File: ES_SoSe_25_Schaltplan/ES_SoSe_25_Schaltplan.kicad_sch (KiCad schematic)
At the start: 3 parts

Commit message: updated scematic
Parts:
- added U3, U4: ~, symbol es_custom_symbols:SSD1806
- added U5: ~, symbol es_custom_symbols:74HC595
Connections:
- net at A1.11 (D8): now also U5.4 (SCLK)
- net at A1.12 (D9): now also U5.5 (LOAD)
- net at A1.13 (D10): now also U5.3 (SDI)
- net at A1.19 (A0): now also U2.H2 (H)
- net at A1.20 (A1): now also U2.V2 (V)
- net at A1.21 (A2): now also U1.H2 (H)
- net at A1.22 (A3): now also U1.V2 (V)
- net at A1.23 (SDA/A4): now also U3.1 (SDA), U4.1 (SDA)
- net at A1.24 (SCL/A5): now also U3.2 (SCL), U4.2 (SCL)
- net GND: now reaches A1.29 (GND), A1.4 (GND)
- net GND: now also U1.B2A (SEL-), U1.H3 (H-), U1.V3 (V-), U2.B2A (SEL-), U2.H3 (H-), U2.V3 (V-), U3.3 (GND), U4.3 (GND), U5.2 (GND)
- net VCC: now reaches A1.30 (VIN)
- net VCC: now also U1.H1 (H+), U1.V1 (V+), U2.H1 (H+), U2.V1 (V+), U3.4 (Vcc), U4.4 (Vcc), U5.1 (Vcc)
- net at A1.5 (D2): now also U1.B1A (Sel+)
- net at A1.6 (D3): now also U2.B1A (Sel+)
- no-connect marks 2 -> 3
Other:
- note added: "Dashboard Schaltplan"
- note added: "I2C"
- note added: "Joysticks"
- moved on the sheet: A1, U1, U2

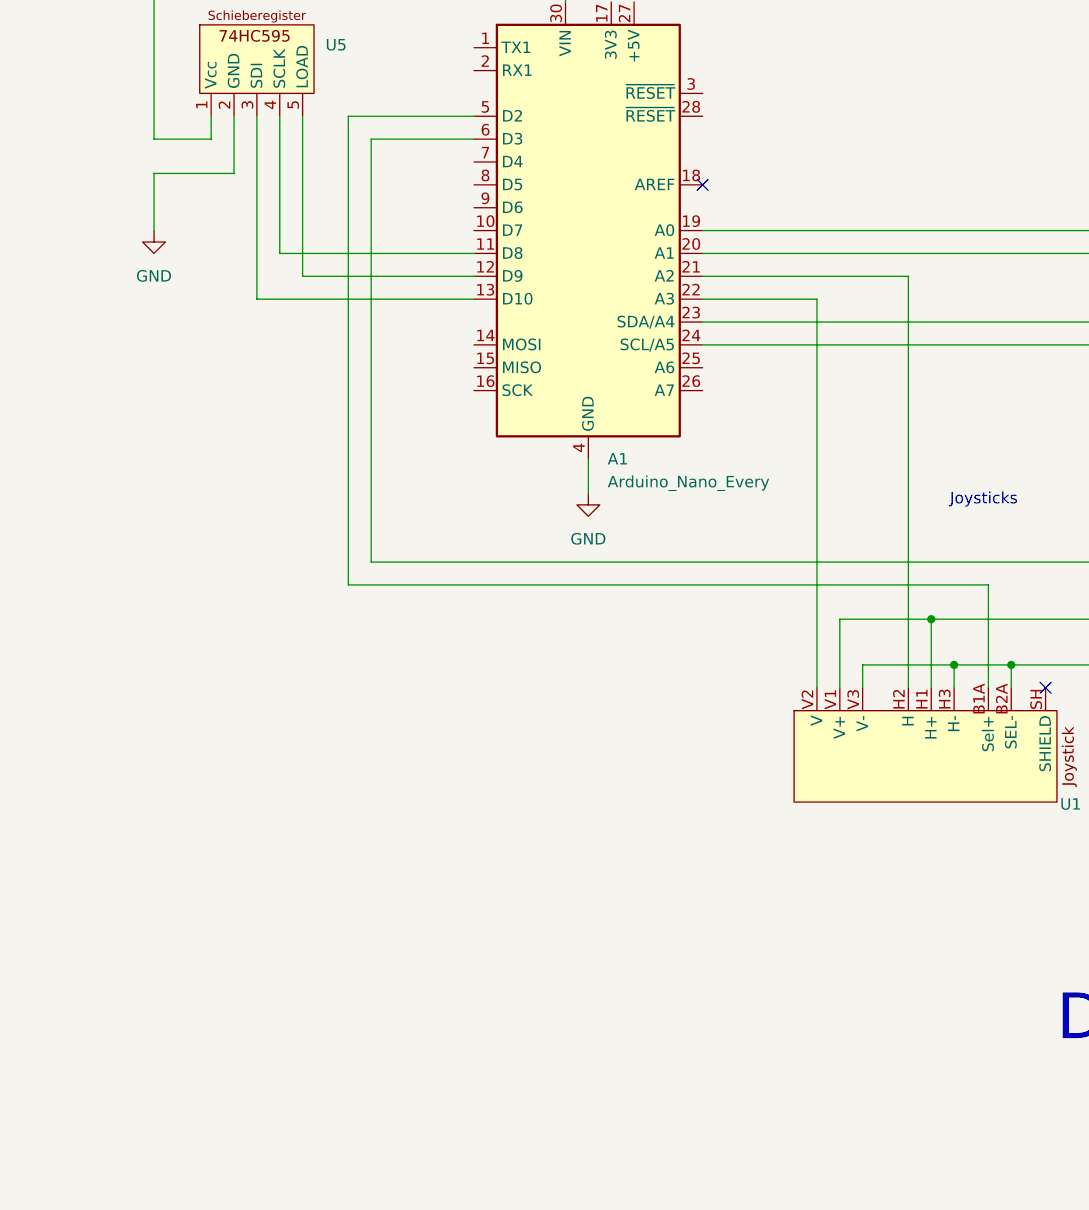
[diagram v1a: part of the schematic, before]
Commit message: added BLE LED
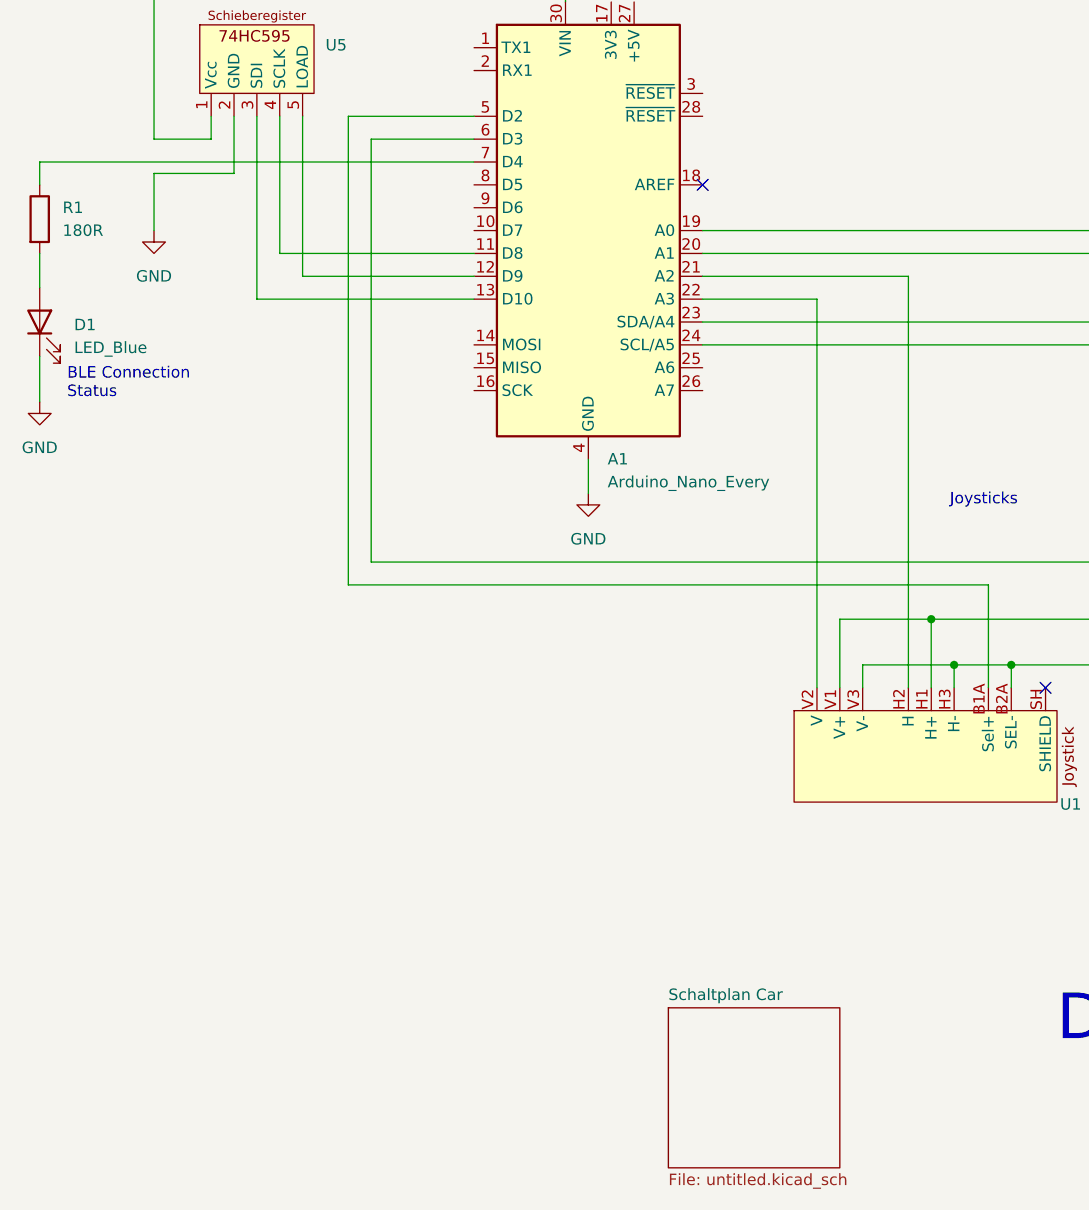
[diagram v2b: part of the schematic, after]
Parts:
- added D1: LED_Blue, symbol Device:LED
- added R1: 180R, symbol Device:R
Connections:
- net GND: now also D1.1 (K)
- net at A1.7 (D4): now also R1.1
- new net: D1.2 (A), R1.2
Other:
- added sheet Schaltplan Car (untitled.kicad_sch)
- note added: "BLE Connection Status"

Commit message: updated scematic
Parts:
- removed A1: Arduino_Nano_Every, Module:Arduino_Nano, symbol MCU_Module:Arduino_Nano_Every
- added A4: Arduino_Nano_33_BLE_Sense_Tile, PCM_arduino-library:Arduino_Nano_Every_Tile, symbol arduino-library:Arduino_Nano_33_BLE_Sense_Tile
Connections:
- net GND: now also A4.GND1 (GND), A4.GND2 (GND)
- net VCC: now also A4.VIN
- net at R1.1: now also A4.D4
- net at U5.4 (SCLK): now also A4.D8
- net at U5.5 (LOAD): now also A4.D9
- net at U5.3 (SDI): now also A4.D10
- net at U2.H2 (H): now also A4.A3
- net at U2.V2 (V): now also A4.A2
- net at U1.H2 (H): now also A4.A1
- net at U1.V2 (V): now also A4.A0
- net at U3.1 (SDA), U4.1 (SDA): now also A4.A4 (A4/SDA)
- net at U3.2 (SCL), U4.2 (SCL): now also A4.A5 (A5/SCL)
- net at U1.B1A (Sel+): now also A4.D2
- net at U2.B1A (Sel+): now also A4.D3
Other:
- moved on the sheet: U3, U4, U5

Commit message: adjusted scematic
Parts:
- removed U5: ~, symbol es_custom_symbols:74HC595
- added U5: ~, symbol es_custom_symbols:SSD1806
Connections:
- net GND: now also U5.3 (GND)
- net VCC: now also U5.4 (Vcc)
- net at A4.D8: now also U5.2 (SCL)
- net at A4.D9: now also U5.1 (SDA)
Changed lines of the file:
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@@
+	(wire
+		(pts
+			(xy 110.49 63.5) (xy 110.49 60.96)
+		)
+		(stroke
+			(width 0)
+			(type default)
+		)
+	)
 	(wire
 		(pts
@@
 	(wire
 		(pts
+			(xy 91.44 73.66) (xy 91.44 52.07)
+		)
+		(stroke
+			(width 0)
+			(type default)
+		)
+	)
+	(wire
+		(pts
 			(xy 118.11 123.19) (xy 118.11 58.42)
 		)
@@
 	(wire
 		(pts
+			(xy 95.25 52.07) (xy 95.25 71.12)
+		)
+		(stroke
+			(width 0)
+			(type default)
+		)
+	)
+	(wire
+		(pts
 			(xy 186.69 120.65) (xy 186.69 81.28)
 		)
@@
 	(wire
 		(pts
-			(xy 101.6 55.88) (xy 101.6 73.66)
-		)
-		(stroke
-			(width 0)
-			(type default)
-		)
-	)
-	(wire
-		(pts
 			(xy 228.6 50.8) (xy 228.6 71.12)
 		)
@@
 	(wire
 		(pts
-			(xy 101.6 73.66) (xy 121.92 73.66)
-		)
-		(stroke
-			(width 0)
-			(type default)
-		)
-	)
-	(wire
-		(pts
 			(xy 209.55 137.16) (xy 209.55 134.62)
 		)
@@
 	(wire
 		(pts
-			(xy 91.44 55.88) (xy 91.44 58.42)
-		)
-		(stroke
-			(width 0)
-			(type default)
-		)
-	)
-	(wire
-		(pts
 			(xy 259.08 58.42) (xy 233.68 58.42)
 		)
@@
 	(wire
 		(pts
-			(xy 96.52 55.88) (xy 96.52 76.2)
+			(xy 95.25 71.12) (xy 121.92 71.12)
 		)
 		(stroke
@@
 	(wire
 		(pts
-			(xy 99.06 55.88) (xy 99.06 71.12)
-		)
-		(stroke
-			(width 0)
-			(type default)
-		)
-	)
-	(wire
-		(pts
 			(xy 236.22 121.92) (xy 236.22 129.54)
 		)
@@
 	(wire
 		(pts
-			(xy 85.09 62.23) (xy 85.09 68.58)
+			(xy 91.44 73.66) (xy 121.92 73.66)
 		)
 		(stroke
@@
 	(wire
 		(pts
+			(xy 110.49 57.15) (xy 104.14 57.15)
+		)
+		(stroke
+			(width 0)
+			(type default)
+		)
+	)
+	(wire
+		(pts
 			(xy 180.34 129.54) (xy 170.18 129.54)
 		)
@@
 	(wire
 		(pts
-			(xy 93.98 62.23) (xy 93.98 55.88)
+			(xy 110.49 60.96) (xy 100.33 60.96)
 		)
 		(stroke
@@
 	(wire
 		(pts
-			(xy 85.09 41.91) (xy 85.09 58.42)
+			(xy 100.33 60.96) (xy 100.33 52.07)
+		)
+		(stroke
+			(width 0)
+			(type default)
+		)
+	)
+	(wire
+		(pts
+			(xy 110.49 46.99) (xy 110.49 57.15)
 		)
 		(stroke
@@
 	(wire
 		(pts
-			(xy 99.06 71.12) (xy 121.92 71.12)
-		)
-		(stroke
-			(width 0)
-			(type default)
-		)
-	)
-	(wire
-		(pts
 			(xy 217.17 58.42) (xy 217.17 63.5)
 		)
@@
 	(wire
 		(pts
+			(xy 104.14 57.15) (xy 104.14 52.07)
+		)
+		(stroke
+			(width 0)
+			(type default)
+		)
+	)
+	(wire
+		(pts
 			(xy 204.47 78.74) (xy 172.72 78.74)
 		)
@@
 	(wire
 		(pts
-			(xy 96.52 76.2) (xy 121.92 76.2)
-		)
-		(stroke
-			(width 0)
-			(type default)
-		)
-	)
-	(wire
-		(pts
-			(xy 85.09 58.42) (xy 91.44 58.42)
-		)
-		(stroke
-			(width 0)
-			(type default)
-		)
-	)
-	(wire
-		(pts
 			(xy 118.11 123.19) (xy 223.52 123.19)
-		)
-		(stroke
-			(width 0)
-			(type default)
-		)
-	)
-	(wire
-		(pts
-			(xy 85.09 62.23) (xy 93.98 62.23)
 		)
 		(stroke
@@
 	(symbol
 		(lib_id "power:GND")
-		(at 85.09 68.58 0)
+		(at 110.49 63.5 0)
 		(unit 1)
 		(exclude_from_sim no)
@@
 		(fields_autoplaced yes)
 		(property "Reference" "#PWR04"
-			(at 85.09 74.93 0)
+			(at 110.49 69.85 0)
 			(effects
 				(font
@@
 		)
 		(property "Value" "GND"
-			(at 85.09 73.66 0)
+			(at 110.49 68.58 0)
 			(effects
 				(font
@@
 		)
 		(property "Footprint" ""
-			(at 85.09 68.58 0)
+			(at 110.49 63.5 0)
 			(effects
 				(font
@@
 		)
 		(property "Datasheet" ""
-			(at 85.09 68.58 0)
+			(at 110.49 63.5 0)
 			(effects
 				(font
@@
 		)
 		(property "Description" "Power symbol creates a global label with name \"GND\" , ground"
-			(at 85.09 68.58 0)
+			(at 110.49 63.5 0)
 			(effects
 				(font
@@
 	)
 	(symbol
+		(lib_name "SSD1806_1")
+		(lib_id "es_custom_symbols:SSD1806")
+		(at 97.79 45.72 0)
+		(unit 1)
+		(exclude_from_sim no)
+		(in_bom yes)
+		(on_board yes)
+		(dnp no)
+		(property "Reference" "U5"
+			(at 106.934 48.768 0)
+			(effects
+				(font
+					(size 1.27 1.27)
+				)
+				(justify left)
+			)
+		)
+		(property "Value" "~"
+			(at 105.41 46.99 0)
+			(effects
+				(font
+					(size 1.27 1.27)
+				)
+				(justify left)
+			)
+		)
+		(property "Footprint" ""
+			(at 97.79 45.72 0)
+			(effects
+				(font
+					(size 1.27 1.27)
+				)
+				(hide yes)
+			)
+		)
+		(property "Datasheet" ""
+			(at 97.79 45.72 0)
+			(effects
+				(font
+					(size 1.27 1.27)
+				)
+				(hide yes)
+			)
+		)
+		(property "Description" ""
+			(at 97.79 45.72 0)
+			(effects
+				(font
+					(size 1.27 1.27)
+				)
+				(hide yes)
+			)
+		)
+		(pin "2"
+		)
+		(pin "3"
+		)
+		(pin "1"
+		)
+		(pin "4"
+		)
+		(instances
+			(project "ES_SoSe_25_Schaltplan"
+				(path "/232146ae-6a38-4d21-b056-d9d96ad8f36d"
+					(reference "U5")
+					(unit 1)
+				)
+			)
+		)
+	)
+	(symbol
 		(lib_id "power:GND")
 		(at 175.26 105.41 0)
@@
 	)
 	(symbol
-		(lib_id "es_custom_symbols:74HC595")
-		(at 96.52 48.26 0)
-		(unit 1)
-		(exclude_from_sim no)
-		(in_bom yes)
-		(on_board yes)
-		(dnp no)
-		(fields_autoplaced yes)
-		(property "Reference" "U5"
-			(at 104.14 47.9783 0)
-			(effects
-				(font
-					(size 1.27 1.27)
-				)
-				(justify left)
-			)
-		)
-		(property "Value" "~"
-			(at 104.14 49.8834 0)
-			(effects
-				(font
-					(size 1.27 1.27)
-				)
-				(justify left)
-			)
-		)
-		(property "Footprint" ""
-			(at 96.52 48.26 0)
-			(effects
-				(font
-					(size 1.27 1.27)
-				)
-				(hide yes)
-			)
-		)
-		(property "Datasheet" ""
-			(at 96.52 48.26 0)
-			(effects
-				(font
-					(size 1.27 1.27)
-				)
-				(hide yes)
-			)
-		)
-		(property "Description" ""
-			(at 96.52 48.26 0)
-			(effects
-				(font
-					(size 1.27 1.27)
-				)
-				(hide yes)
-			)
-		)
-		(pin "3"
-		)
-		(pin "5"
-		)
-		(pin "4"
-		)
-		(pin "1"
-		)
-		(pin "2"
-		)
-		(instances
-			(project ""
-				(path "/232146ae-6a38-4d21-b056-d9d96ad8f36d"
-					(reference "U5")
-					(unit 1)
-				)
-			)
-		)
-	)
-	(symbol
 		(lib_id "es_custom_symbols:Joystick")
 		(at 208.28 143.51 90)
@@
 	(symbol
 		(lib_id "power:VCC")
-		(at 85.09 41.91 0)
+		(at 110.49 46.99 0)
 		(unit 1)
 		(exclude_from_sim no)
@@
 		(fields_autoplaced yes)
 		(property "Reference" "#PWR05"
-			(at 85.09 45.72 0)
+			(at 110.49 50.8 0)
 			(effects
 				(font
@@
 		)
 		(property "Value" "VCC"
-			(at 85.09 36.83 0)
+			(at 110.49 41.91 0)
 			(effects
 				(font
@@
 		)
 		(property "Footprint" ""
-			(at 85.09 41.91 0)
+			(at 110.49 46.99 0)
 			(effects
 				(font
@@
 		)
 		(property "Datasheet" ""
-			(at 85.09 41.91 0)
+			(at 110.49 46.99 0)
 			(effects
 				(font
@@
 		)
 		(property "Description" "Power symbol creates a global label with name \"VCC\""
-			(at 85.09 41.91 0)
-			(effects
-				(font
+			(at 110.49 46.99 0)
+			(effects
+				(font

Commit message: edited ble and scematic
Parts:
- added D4, D5, D6, D7, D8: LED, symbol Device:LED
- added R4, R5, R6, R7, R8: 180R, symbol Device:R
- added SW1, SW2, SW3, SW4: ~, symbol Switch:SW_SPST
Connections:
- net GND: now also D4.1 (K), D5.1 (K), D6.1 (K), D7.1 (K), D8.1 (K), SW1.2 (B), SW2.2 (B), SW3.2 (B), SW4.2 (B)
- net at A4.A6: now also R4.1
- net at A4.A7: now also R5.1
- net at A4.D10: now also SW4.1 (A)
- net at A4.D11 (D11_MOSI): now also R6.1
- net at A4.D12 (D12_MISO): now also R7.1
- net at A4.D13 (D13_SCK): now also R8.1
- net at A4.D5: now also SW1.1 (A)
- net at A4.D6: now also SW2.1 (A)
- net at A4.D7: now also SW3.1 (A)
- new net: D5.2 (A), R5.2
- new net: D6.2 (A), R6.2
- new net: D4.2 (A), R4.2
- new net: D8.2 (A), R8.2
- new net: D7.2 (A), R7.2
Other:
- moved on the sheet: D1, R1, U5
